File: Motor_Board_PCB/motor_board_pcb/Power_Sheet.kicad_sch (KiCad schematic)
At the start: 18 parts, among them J6 Barrel_Jack_MountingPin, U5 AP2112K-3.3TRG1, U6 AP63205WU-7

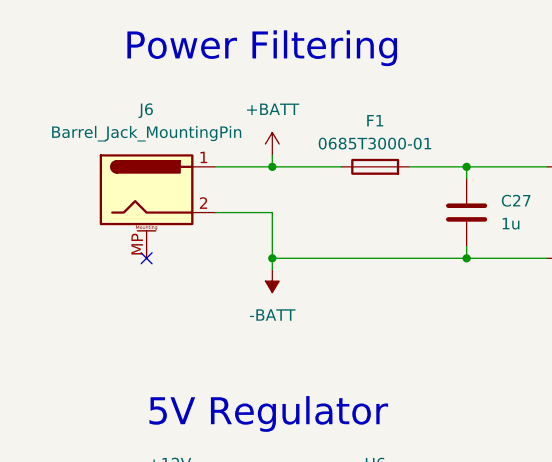
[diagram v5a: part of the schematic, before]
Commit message: Added cap on accel chip and switched power connector
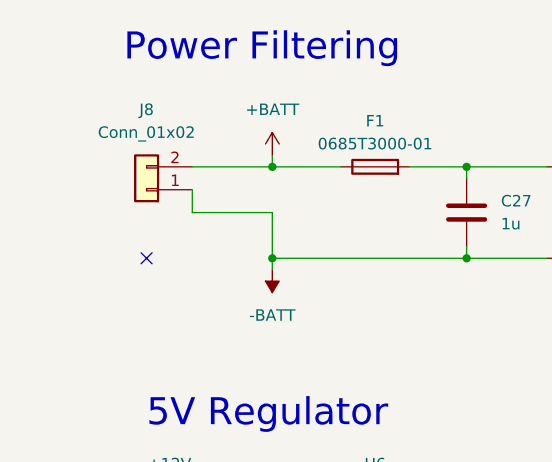
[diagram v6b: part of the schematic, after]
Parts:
- removed J6: Barrel_Jack_MountingPin, Connector_BarrelJack:BarrelJack_CUI_PJ-063AH_Horizontal, symbol Connector:Barrel_Jack_MountingPin
- added J8: Conn_01x02, Connector_PinHeader_2.54mm:PinHeader_1x02_P2.54mm_Vertical, symbol Connector_Generic:Conn_01x02
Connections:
- net +BATT: now also J8.2 (Pin_2)
- net -BATT: now also J8.1 (Pin_1)
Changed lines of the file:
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@@
+    (stroke (width 0) (type default))
+  )
+  (wire (pts (xy 43.18 53.34) (xy 43.18 50.8))
     (stroke (width 0) (type default))
   )
@@
     (stroke (width 0) (type default))
   )
-  (wire (pts (xy 45.72 48.26) (xy 52.07 48.26))
+  (wire (pts (xy 43.18 48.26) (xy 52.07 48.26))
     (stroke (width 0) (type default))
   )
@@
     (stroke (width 0) (type default))
   )
-  (wire (pts (xy 45.72 53.34) (xy 52.07 53.34))
+  (wire (pts (xy 43.18 53.34) (xy 52.07 53.34))
     (stroke (width 0) (type default))
   )
@@
     )
   )
-  (symbol (lib_id "Connector:Barrel_Jack_MountingPin") (at 38.1 50.8 0) (unit 1)
-    (in_bom yes) (on_board yes) (dnp no) (fields_autoplaced)
-    (property "Reference" "J6" (at 38.1 41.91 0)
-      (effects (font (size 1.27 1.27)))
-    )
-    (property "Value" "Barrel_Jack_MountingPin" (at 38.1 44.45 0)
-      (effects (font (size 1.27 1.27)))
-    )
-    (property "Footprint" "Connector_BarrelJack:BarrelJack_CUI_PJ-063AH_Horizontal" (at 39.37 51.816 0)
-      (effects (font (size 1.27 1.27)) hide)
-    )
-    (property "Datasheet" "~" (at 39.37 51.816 0)
-      (effects (font (size 1.27 1.27)) hide)
-    )
-    (pin "1")
-    (pin "2")
-    (pin "MP")
-    (instances
-      (project "motor_board_pcb"
-        (path "/4ad82a24-c992-45c9-b523-12e12bcd6ced/8b03500d-82ba-403b-affc-552426d5b4ea"
-          (reference "J6") (unit 1)
-        )
-      )
-    )
-  )
   (symbol (lib_id "DLW5BTM251TQ2L:DLW5BTM251TQ2L") (at 92.71 53.34 0) (unit 1)
     (in_bom yes) (on_board yes) (dnp no) (fields_autoplaced)
@@
         )
       )
+    )
+  )
+  (symbol (lib_id "Connector_Generic:Conn_01x02") (at 38.1 50.8 180) (unit 1)
+    (in_bom yes) (on_board yes) (dnp no) (fields_autoplaced)
+    (property "Reference" "J8" (at 38.1 41.91 0)
+      (effects (font (size 1.27 1.27)))
+    )
+    (property "Value" "Conn_01x02" (at 38.1 44.45 0)
+      (effects (font (size 1.27 1.27)))
+    )
+    (property "Footprint" "Connector_PinHeader_2.54mm:PinHeader_1x02_P2.54mm_Vertical" (at 38.1 50.8 0)
+      (effects (font (size 1.27 1.27)) hide)
+    )
+    (property "Datasheet" "~" (at 38.1 50.8 0)
+      (effects (font (size 1.27 1.27)) hide)
+    )
+    (pin "1")
+    (pin "2")
+    (instances
+      (project "motor_board_pcb"
+        (path "/4ad82a24-c992-45c9-b523-12e12bcd6ced/996060af-581e-425f-9e10-26ee39d5a960"
+          (reference "J8") (unit 1)
+        )
+        (path "/4ad82a24-c992-45c9-b523-12e12bcd6ced/8b03500d-82ba-403b-affc-552426d5b4ea"
+          (reference "J3") (unit 1)
+        )
+      )

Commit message: Meeting Changes
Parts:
- removed C24, C25: 1u, Capacitor_SMD:C_0603_1608Metric, symbol Device:C
- removed U5: AP2112K-3.3TRG1, Package_TO_SOT_SMD:SOT-23-5, symbol Regulator_Linear:AP2112K-3.3
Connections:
- net +BATT: now also J8.1 (Pin_1); no longer J8.2 (Pin_2)
- net -BATT: now also J8.2 (Pin_2); no longer J8.1 (Pin_1)
- no-connect marks 1 -> 0
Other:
- note removed: "3V3 Regulator"

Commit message: Meeting additional changes
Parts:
- added D4: PMEG6020AELRX, Diode_SMD:Nexperia_CFP3_SOD-123W, symbol Diode:PMEG6020AELR
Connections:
- new net VUSB: D4.2 (A)
- new net VUSB_DIODE: D4.1 (K)
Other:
- note added: "SCHOTTKY FOR USB OVERVOLTAGE PROTECTION"
- moved on the sheet: C23, C26, C28, C29, L3, U6
